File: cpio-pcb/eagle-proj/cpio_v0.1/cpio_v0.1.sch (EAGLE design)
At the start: 60 parts

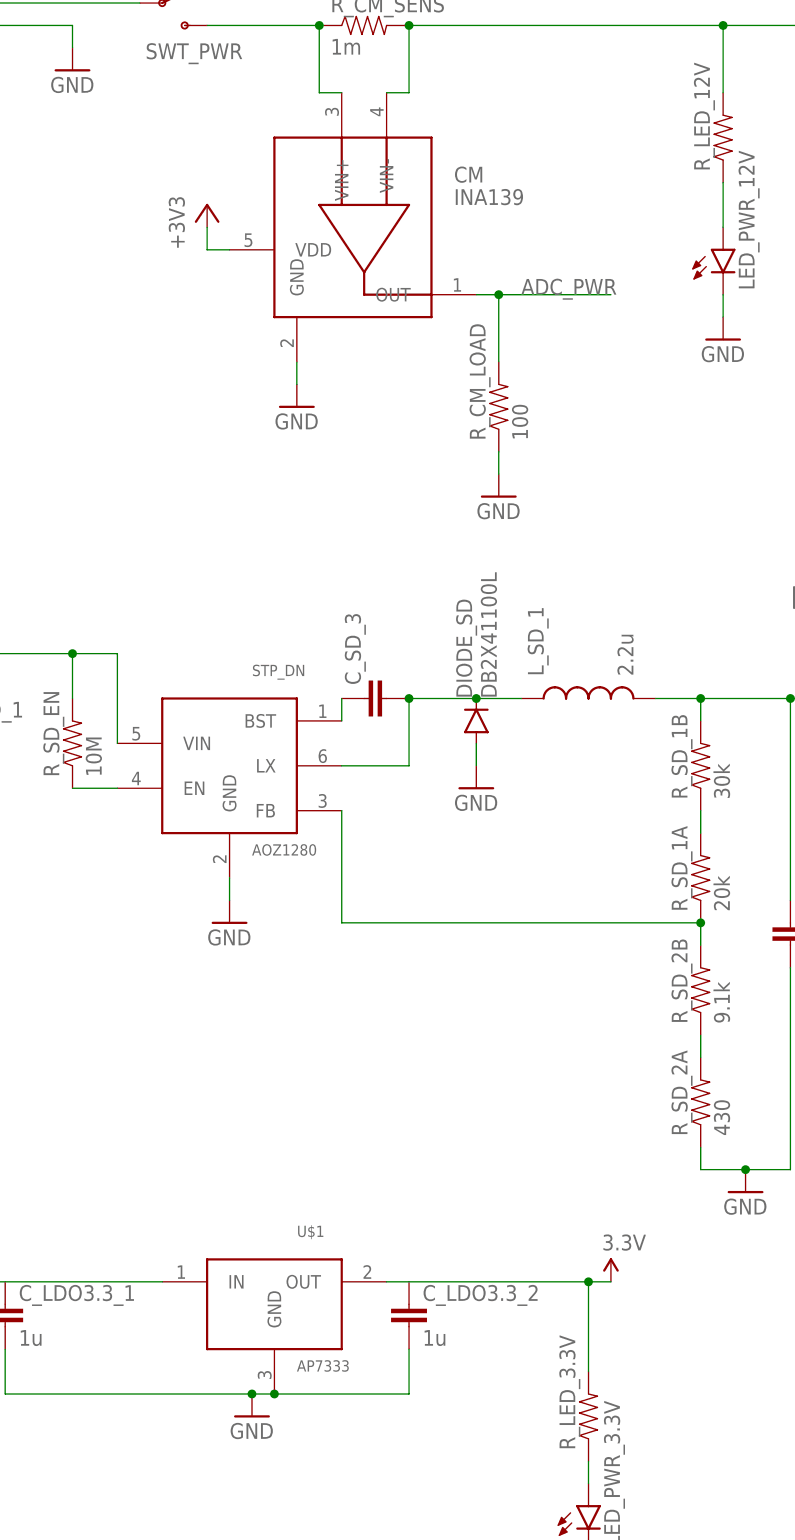
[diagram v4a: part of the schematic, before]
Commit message: smaller Typo corrections
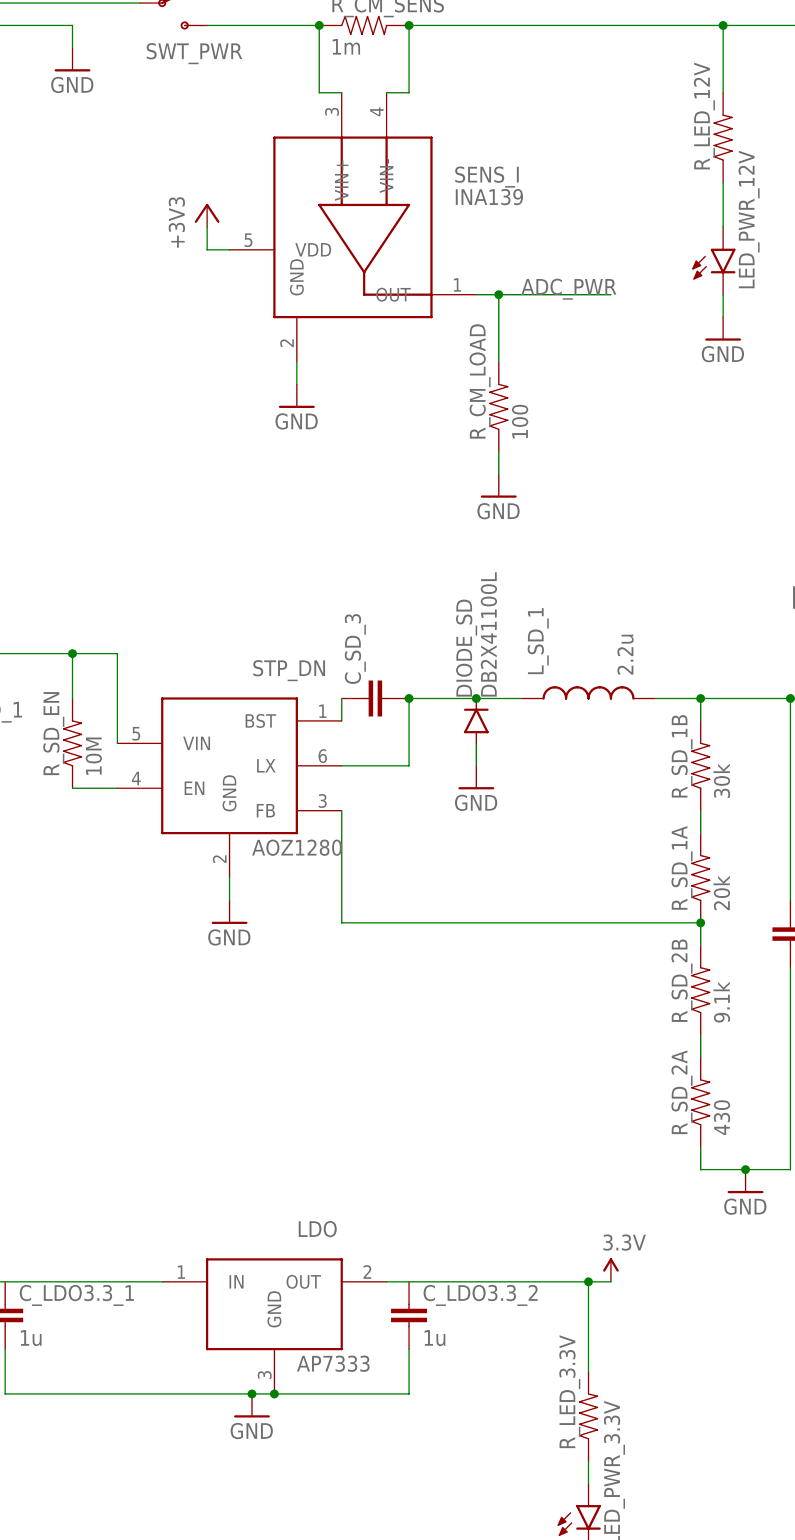
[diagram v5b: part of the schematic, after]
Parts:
- renumbered CM to SENS_I, U$1 to LDO
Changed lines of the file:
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@@
 <part name="GND9" library="SparkFun-Aesthetics" deviceset="GND" device=""/>
 <part name="LED_PWR_12V" library="SparkFun-LED" deviceset="LED" device="1206"/>
-<part name="CM" library="cpio" deviceset="INA139" device=""/>
+<part name="SENS_I" library="cpio" deviceset="INA139" device=""/>
 <part name="R_LED_12V" library="SparkFun-Passives" deviceset="RESISTOR" device="0805-RES"/>
 <part name="R_CM_SENS" library="SparkFun-Passives" deviceset="RESISTOR" device="0805-RES" value="1m"/>
@@
 <part name="SUPPLY1" library="SparkFun-Aesthetics" deviceset="12V" device=""/>
 <part name="SWT_PWR" library="cpio" deviceset="500SSP1S2" device=""/>
-<part name="STP_DN" library="cpio" deviceset="AOZ1280" device=""/>
 <part name="SUPPLY2" library="SparkFun-Aesthetics" deviceset="12V" device=""/>
 <part name="C_SD_1" library="SparkFun-Passives" deviceset="CAP" device="0805" value="4.7u"/>
@@
 <part name="R_SD_2B" library="SparkFun-Passives" deviceset="RESISTOR" device="0805-RES" value="9.1k"/>
 <part name="R_SD_2A" library="SparkFun-Passives" deviceset="RESISTOR" device="0805-RES" value="430"/>
-<part name="U$1" library="cpio" deviceset="AP7333" device=""/>
 <part name="C_LDO3.3_1" library="SparkFun-Passives" deviceset="CAP" device="0805" value="1u"/>
 <part name="C_LDO3.3_2" library="SparkFun-Passives" deviceset="CAP" device="0805" value="1u"/>
@@
 <part name="R_SPI_2" library="SparkFun-Passives" deviceset="RESISTOR" device="0805-RES" value="10k"/>
 <part name="R_SPI_3" library="SparkFun-Passives" deviceset="RESISTOR" device="0805-RES" value="10k"/>
+<part name="STP_DN" library="cpio" deviceset="AOZ1280" device=""/>
+<part name="LDO" library="cpio" deviceset="AP7333" device=""/>
 </parts>
 <sheets>
@@
 <instance part="GND9" gate="1" x="63.5" y="2.54"/>
 <instance part="LED_PWR_12V" gate="G$1" x="137.16" y="-17.78"/>
-<instance part="CM" gate="G$1" x="96.52" y="-15.24"/>
+<instance part="SENS_I" gate="G$1" x="96.52" y="-15.24"/>
 <instance part="R_LED_12V" gate="G$1" x="137.16" y="-5.08" rot="R90"/>
 <instance part="R_CM_SENS" gate="G$1" x="96.52" y="7.62"/>
@@
 <instance part="SUPPLY1" gate="G$1" x="269.24" y="7.62"/>
 <instance part="SWT_PWR" gate="G$1" x="73.66" y="10.16"/>
-<instance part="STP_DN" gate="G$1" x="68.58" y="-73.66"/>
 <instance part="SUPPLY2" gate="G$1" x="48.26" y="-63.5"/>
 <instance part="C_SD_1" gate="G$1" x="48.26" y="-73.66"/>
@@
 <instance part="R_SD_2B" gate="G$1" x="134.62" y="-101.6" rot="R90"/>
 <instance part="R_SD_2A" gate="G$1" x="134.62" y="-114.3" rot="R90"/>
-<instance part="U$1" gate="G$1" x="73.66" y="-134.62"/>
 <instance part="C_LDO3.3_1" gate="G$1" x="55.88" y="-139.7"/>
 <instance part="C_LDO3.3_2" gate="G$1" x="101.6" y="-139.7"/>
@@
 <instance part="R_SPI_2" gate="G$1" x="-66.04" y="-15.24" rot="R90"/>
 <instance part="R_SPI_3" gate="G$1" x="20.32" y="-20.32" rot="R90"/>
+<instance part="STP_DN" gate="G$1" x="68.58" y="-73.66"/>
+<instance part="LDO" gate="G$1" x="73.66" y="-134.62"/>
 </instances>
 <busses>
@@
 </segment>
 <segment>
-<pinref part="CM" gate="G$1" pin="GND"/>
+<pinref part="SENS_I" gate="G$1" pin="GND"/>
 <pinref part="GND11" gate="1" pin="GND"/>
 <wire x1="88.9" y1="-30.48" x2="88.9" y2="-33.02" width="0.1524" layer="91"/>
@@
 </segment>
 <segment>
-<pinref part="STP_DN" gate="G$1" pin="GND"/>
 <pinref part="GND14" gate="1" pin="GND"/>
 <wire x1="81.28" y1="-88.9" x2="81.28" y2="-91.44" width="0.1524" layer="91"/>
+<pinref part="STP_DN" gate="G$1" pin="GND"/>
 </segment>
 <segment>
@@
 <segment>
 <pinref part="C_LDO3.3_1" gate="G$1" pin="2"/>
-<pinref part="U$1" gate="G$1" pin="GND"/>
 <wire x1="55.88" y1="-142.24" x2="55.88" y2="-147.32" width="0.1524" layer="91"/>
 <wire x1="55.88" y1="-147.32" x2="83.82" y2="-147.32" width="0.1524" layer="91"/>
@@
 <wire x1="86.36" y1="-147.32" x2="101.6" y2="-147.32" width="0.1524" layer="91"/>
 <wire x1="101.6" y1="-147.32" x2="101.6" y2="-142.24" width="0.1524" layer="91"/>
-<junction x="86.36" y="-147.32"/>
 <pinref part="GND19" gate="1" pin="GND"/>
 <junction x="83.82" y="-147.32"/>
+<pinref part="LDO" gate="G$1" pin="GND"/>
+<junction x="86.36" y="-147.32"/>
 </segment>
 <segment>
@@
 <pinref part="+3V3" gate="G$1" pin="+3V3"/>
 <wire x1="78.74" y1="-15.24" x2="78.74" y2="-17.78" width="0.1524" layer="91"/>
-<pinref part="CM" gate="G$1" pin="VDD"/>
+<pinref part="SENS_I" gate="G$1" pin="VDD"/>
 <wire x1="78.74" y1="-17.78" x2="81.28" y2="-17.78" width="0.1524" layer="91"/>
 </segment>
@@
 <net name="ADC_PWR" class="0">
 <segment>
-<pinref part="CM" gate="G$1" pin="OUT"/>
+<pinref part="SENS_I" gate="G$1" pin="OUT"/>
 <wire x1="109.22" y1="-22.86" x2="111.76" y2="-22.86" width="0.1524" layer="91"/>
 <pinref part="R_CM_LOAD" gate="G$1" pin="2"/>
@@
 <pinref part="R_CM_SENS" gate="G$1" pin="1"/>
 <wire x1="78.74" y1="7.62" x2="91.44" y2="7.62" width="0.1524" layer="91"/>
-<pinref part="CM" gate="G$1" pin="VIN+"/>
+<pinref part="SENS_I" gate="G$1" pin="VIN+"/>
 <wire x1="91.44" y1="0" x2="93.98" y2="0" width="0.1524" layer="91"/>
 <wire x1="91.44" y1="7.62" x2="91.44" y2="0" width="0.1524" layer="91"/>
@@
 <pinref part="SUPPLY2" gate="G$1" pin="12V"/>
 <wire x1="48.26" y1="-68.58" x2="48.26" y2="-63.5" width="0.1524" layer="91"/>
-<pinref part="STP_DN" gate="G$1" pin="VIN"/>
 <wire x1="68.58" y1="-73.66" x2="68.58" y2="-63.5" width="0.1524" layer="91"/>
 <wire x1="68.58" y1="-63.5" x2="63.5" y2="-63.5" width="0.1524" layer="91"/>
@@
 <wire x1="63.5" y1="-63.5" x2="63.5" y2="-68.58" width="0.1524" layer="91"/>
 <junction x="63.5" y="-63.5"/>
-</segment>
-<segment>
-<pinref part="CM" gate="G$1" pin="VIN-"/>
+<pinref part="STP_DN" gate="G$1" pin="VIN"/>
+</segment>
+<segment>
+<pinref part="SENS_I" gate="G$1" pin="VIN-"/>
 <wire x1="99.06" y1="0" x2="101.6" y2="0" width="0.1524" layer="91"/>
 <pinref part="R_CM_SENS" gate="G$1" pin="2"/>
@@
 <net name="N$6" class="0">
 <segment>
-<pinref part="STP_DN" gate="G$1" pin="EN"/>
 <pinref part="R_SD_EN" gate="G$1" pin="1"/>
 <wire x1="68.58" y1="-78.74" x2="63.5" y2="-78.74" width="0.1524" layer="91"/>
+<pinref part="STP_DN" gate="G$1" pin="EN"/>
 </segment>
 </net>
@@
 <segment>
 <pinref part="C_SD_3" gate="G$1" pin="1"/>
+<wire x1="93.98" y1="-68.58" x2="93.98" y2="-71.12" width="0.1524" layer="91"/>
 <pinref part="STP_DN" gate="G$1" pin="BST"/>
-<wire x1="93.98" y1="-68.58" x2="93.98" y2="-71.12" width="0.1524" layer="91"/>
 </segment>
 </net>
@@
 <junction x="101.6" y="-68.58"/>
 <wire x1="101.6" y1="-76.2" x2="101.6" y2="-68.58" width="0.1524" layer="91"/>
-<pinref part="STP_DN" gate="G$1" pin="LX"/>
 <wire x1="93.98" y1="-76.2" x2="101.6" y2="-76.2" width="0.1524" layer="91"/>
 <pinref part="L_SD_1" gate="G$1" pin="1"/>
 <wire x1="109.22" y1="-68.58" x2="114.3" y2="-68.58" width="0.1524" layer="91"/>
 <junction x="109.22" y="-68.58"/>
+<pinref part="STP_DN" gate="G$1" pin="LX"/>
 </segment>
 </net>
@@
 </segment>
 <segment>
-<pinref part="U$1" gate="G$1" pin="IN"/>
 <wire x1="73.66" y1="-134.62" x2="53.34" y2="-134.62" width="0.1524" layer="91"/>
 <pinref part="SUPPLY4" gate="G$1" pin="5V"/>
+<pinref part="LDO" gate="G$1" pin="IN"/>
 </segment>
 <segment>
@@
 <net name="N$12" class="0">
 <segment>
-<pinref part="STP_DN" gate="G$1" pin="FB"/>
 <pinref part="R_SD_1A" gate="G$1" pin="1"/>
 <wire x1="93.98" y1="-81.28" x2="93.98" y2="-93.98" width="0.1524" layer="91"/>
@@
 <wire x1="134.62" y1="-93.98" x2="134.62" y2="-96.52" width="0.1524" layer="91"/>
 <junction x="134.62" y="-93.98"/>
+<pinref part="STP_DN" gate="G$1" pin="FB"/>
 </segment>
 </net>
@@
 <net name="3.3V" class="0">
 <segment>
-<pinref part="U$1" gate="G$1" pin="OUT"/>
 <wire x1="99.06" y1="-134.62" x2="121.92" y2="-134.62" width="0.1524" layer="91"/>
 <pinref part="SUPPLY5" gate="G$1" pin="3.3V"/>
@@
 <wire x1="121.92" y1="-144.78" x2="121.92" y2="-134.62" width="0.1524" layer="91"/>
 <junction x="121.92" y="-134.62"/>
-</segment>
-<segment>
+<pinref part="LDO" gate="G$1" pin="OUT"/>
+</segment>
+<segment>

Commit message: schematic ready for UX
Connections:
- new net GPIO4: R_1WIRE.1
- new net N$23: R_HSS_PROT_0.1
- new net N$36: R_HSS_PROT_1.1
- new net N$37: R_HSS_PROT_2.1
- new net N$38: R_HSS_PROT_3.1
- new net N$39: R_SS_PROT0.1
- new net N$40: R_SS_PROT1.1
- new net N$41: R_SS_PROT2.1
- new net N$42: R_SS_PROT3.1
- new net PWM0: JP1.12
- net 1WIRE: no longer JP1.12, R_1WIRE.1
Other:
- note added: "To which GPIOs?!"
- moved on the sheet: R_1WIRE, R_SPI_3
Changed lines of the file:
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@@
 <text x="251.46" y="17.78" size="2.54" layer="97">Load Diode missing!</text>
 <text x="177.8" y="-198.12" size="2.54" layer="97">Plugs for potential pH Sensors missing!</text>
+<text x="193.04" y="-10.16" size="2.54" layer="97" rot="R180">To which GPIOs?!</text>
+<text x="226.06" y="-99.06" size="2.54" layer="97" rot="R180">To which GPIOs?!</text>
 </plain>
 <instances>
@@
 <instance part="R_I2C_0" gate="G$1" x="-73.66" y="2.54" rot="R90"/>
 <instance part="R_I2C_1" gate="G$1" x="-66.04" y="5.08" rot="R90"/>
-<instance part="R_1WIRE" gate="G$1" x="12.7" y="-5.08" rot="R90"/>
-<instance part="SUPPLY12" gate="G$1" x="12.7" y="2.54"/>
+<instance part="R_1WIRE" gate="G$1" x="-81.28" y="0" rot="R90"/>
+<instance part="SUPPLY12" gate="G$1" x="15.24" y="-12.7"/>
 <instance part="SENS_HUM_0" gate="G$1" x="322.58" y="-177.8" rot="R180"/>
 <instance part="SENS_HUM_1" gate="G$1" x="322.58" y="-198.12" rot="R180"/>
@@
 <instance part="R_SPI_1" gate="G$1" x="-73.66" y="-17.78" rot="R90"/>
 <instance part="R_SPI_2" gate="G$1" x="-66.04" y="-15.24" rot="R90"/>
-<instance part="R_SPI_3" gate="G$1" x="20.32" y="-20.32" rot="R90"/>
+<instance part="R_SPI_3" gate="G$1" x="15.24" y="-20.32" rot="R90"/>
 <instance part="STP_DN" gate="G$1" x="68.58" y="-73.66"/>
 <instance part="LDO" gate="G$1" x="73.66" y="-134.62"/>
@@
 <net name="GPIO4" class="0">
 <segment>
-<wire x1="-43.18" y1="-5.08" x2="-48.26" y2="-5.08" width="0.1524" layer="91"/>
 <label x="-48.26" y="-5.08" size="1.778" layer="95"/>
+<pinref part="R_1WIRE" gate="G$1" pin="1"/>
+<wire x1="-43.18" y1="-5.08" x2="-81.28" y2="-5.08" width="0.1524" layer="91"/>
 </segment>
 </net>
@@
 <pinref part="JP1" gate="G$1" pin="24"/>
 <pinref part="R_SPI_3" gate="G$1" pin="1"/>
-<wire x1="-17.78" y1="-25.4" x2="20.32" y2="-25.4" width="0.1524" layer="91"/>
+<wire x1="-17.78" y1="-25.4" x2="15.24" y2="-25.4" width="0.1524" layer="91"/>
 </segment>
 <segment>
@@
 <pinref part="JP1" gate="G$1" pin="1"/>
 <wire x1="-58.42" y1="2.54" x2="-33.02" y2="2.54" width="0.1524" layer="91"/>
+<pinref part="R_1WIRE" gate="G$1" pin="2"/>
+<wire x1="-81.28" y1="5.08" x2="-81.28" y2="12.7" width="0.1524" layer="91"/>
+<wire x1="-81.28" y1="12.7" x2="-73.66" y2="12.7" width="0.1524" layer="91"/>
+<junction x="-73.66" y="12.7"/>
 </segment>
 <segment>
 <pinref part="SUPPLY12" gate="G$1" pin="3.3V"/>
-<pinref part="R_1WIRE" gate="G$1" pin="2"/>
-<wire x1="12.7" y1="2.54" x2="12.7" y2="0" width="0.1524" layer="91"/>
 <pinref part="R_SPI_3" gate="G$1" pin="2"/>
-<wire x1="20.32" y1="-15.24" x2="20.32" y2="2.54" width="0.1524" layer="91"/>
-<wire x1="20.32" y1="2.54" x2="12.7" y2="2.54" width="0.1524" layer="91"/>
-<junction x="12.7" y="2.54"/>
+<wire x1="15.24" y1="-15.24" x2="15.24" y2="-12.7" width="0.1524" layer="91"/>
 </segment>
 <segment>
@@
 <label x="292.1" y="-116.84" size="1.778" layer="95"/>
 </segment>
-<segment>
-<label x="-17.78" y="-10.16" size="1.778" layer="95"/>
-<pinref part="JP1" gate="G$1" pin="12"/>
-<pinref part="R_1WIRE" gate="G$1" pin="1"/>
-<wire x1="-17.78" y1="-10.16" x2="12.7" y2="-10.16" width="0.1524" layer="91"/>
-</segment>
 </net>
 <net name="N$14" class="0">
@@
 </segment>
 </net>
+<net name="PWM0" class="0">
+<segment>
+<pinref part="JP1" gate="G$1" pin="12"/>
+<wire x1="-17.78" y1="-10.16" x2="-2.54" y2="-10.16" width="0.1524" layer="91"/>
+<label x="-17.78" y="-10.16" size="1.778" layer="95"/>
+</segment>
+</net>
+<net name="N$23" class="0">
+<segment>
+<pinref part="R_HSS_PROT_0" gate="G$1" pin="1"/>
+<wire x1="190.5" y1="0" x2="177.8" y2="0" width="0.1524" layer="91"/>
+</segment>
+</net>
+<net name="N$36" class="0">
+<segment>
+<pinref part="R_HSS_PROT_1" gate="G$1" pin="1"/>
+<wire x1="200.66" y1="-2.54" x2="177.8" y2="-2.54" width="0.1524" layer="91"/>
+</segment>
+</net>
+<net name="N$37" class="0">
+<segment>
+<pinref part="R_HSS_PROT_2" gate="G$1" pin="1"/>
+<wire x1="210.82" y1="-5.08" x2="177.8" y2="-5.08" width="0.1524" layer="91"/>
+</segment>
+</net>
+<net name="N$38" class="0">
+<segment>
+<pinref part="R_HSS_PROT_3" gate="G$1" pin="1"/>
+<wire x1="220.98" y1="-7.62" x2="177.8" y2="-7.62" width="0.1524" layer="91"/>
+</segment>
+</net>
+<net name="N$39" class="0">
+<segment>
+<pinref part="R_SS_PROT0" gate="G$1" pin="1"/>
+<wire x1="223.52" y1="-81.28" x2="210.82" y2="-81.28" width="0.1524" layer="91"/>
+</segment>
+</net>
+<net name="N$40" class="0">
+<segment>
+<pinref part="R_SS_PROT1" gate="G$1" pin="1"/>
+<wire x1="228.6" y1="-86.36" x2="210.82" y2="-86.36" width="0.1524" layer="91"/>
+</segment>
+</net>
+<net name="N$41" class="0">
+<segment>
+<pinref part="R_SS_PROT2" gate="G$1" pin="1"/>
+<wire x1="233.68" y1="-91.44" x2="210.82" y2="-91.44" width="0.1524" layer="91"/>
+</segment>
+</net>
+<net name="N$42" class="0">
+<segment>
+<pinref part="R_SS_PROT3" gate="G$1" pin="1"/>
+<wire x1="238.76" y1="-96.52" x2="210.82" y2="-96.52" width="0.1524" layer="91"/>
+</segment>
+</net>
